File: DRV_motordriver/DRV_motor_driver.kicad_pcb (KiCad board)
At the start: 2 copper layers, 80.5 x 46.1 mm, 37 parts, among them J1 jumper, J2 jumper, J3 Conn_01x02, J4 Conn_01x02, J5 Conn_01x02, J6 Conn_01x02, J7 Conn_01x02, Q1 NMOS, Q2 NMOS, Q3 NMOS, Q4 NMOS, Q5 NMOS, Q6 NMOS, Q7 NMOS, Q8 NMOS, U1 DRV8701PRGER, U2 DRV8701PRGER

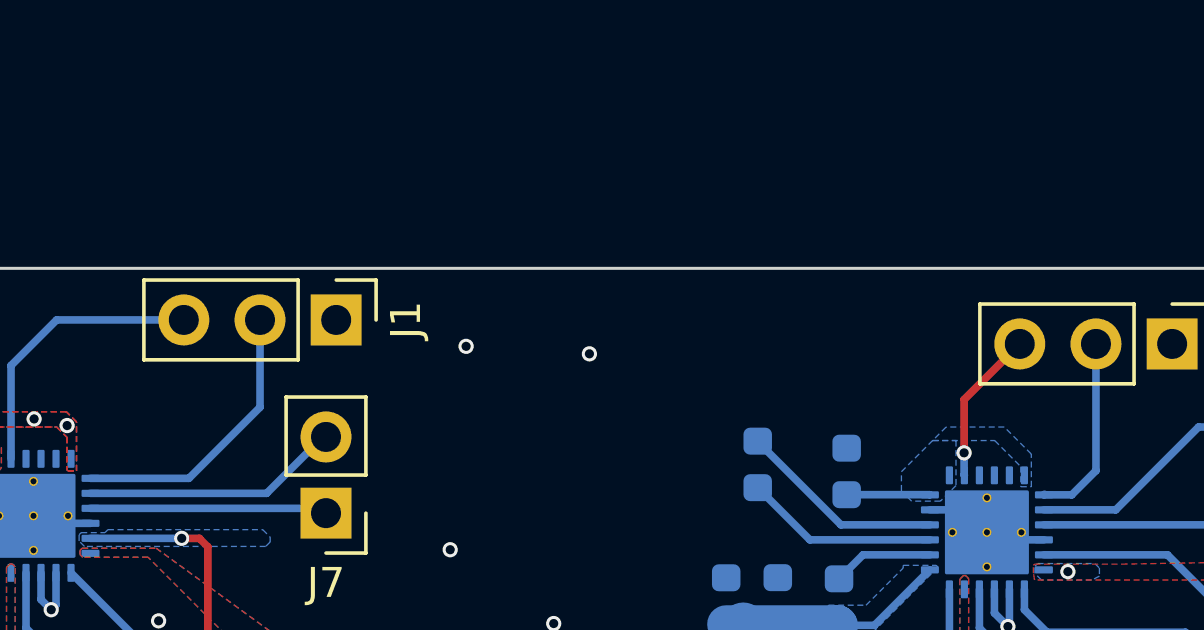
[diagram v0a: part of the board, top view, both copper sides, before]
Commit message: add readme and update on DRV motor driver
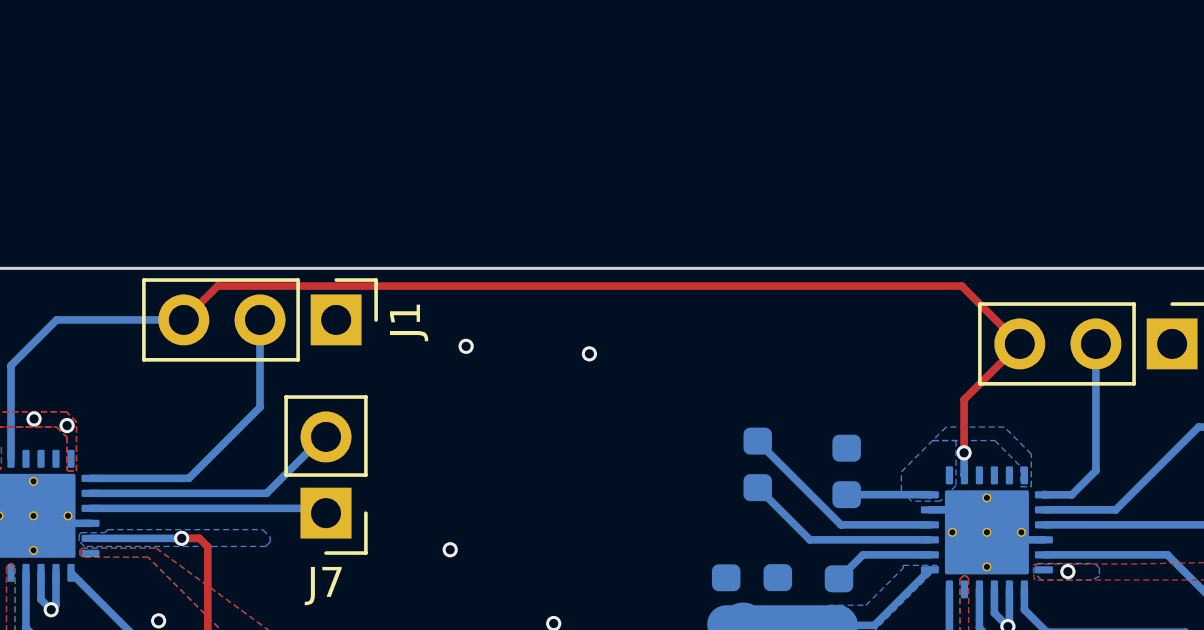
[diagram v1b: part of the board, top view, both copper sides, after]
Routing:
- net +3.3V: track 14.7 -> 43.8 mm
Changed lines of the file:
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@@
+	)
+	(segment
+		(start 77.539401 61.5806)
+		(end 76.410001 62.71)
+		(width 0.254)
+		(layer "F.Cu")
+		(net 14)
+	)
+	(segment
+		(start 102.345601 61.5806)
+		(end 77.539401 61.5806)
+		(width 0.254)
+		(layer "F.Cu")
+		(net 14)
 	)
 	(segment
@@
 		(width 0.254)
 		(layer "F.Cu")
+		(net 14)
+	)
+	(segment
+		(start 104.275001 63.51)
+		(end 102.345601 61.5806)
+		(width 0.254)
+		(layer "F.Cu")

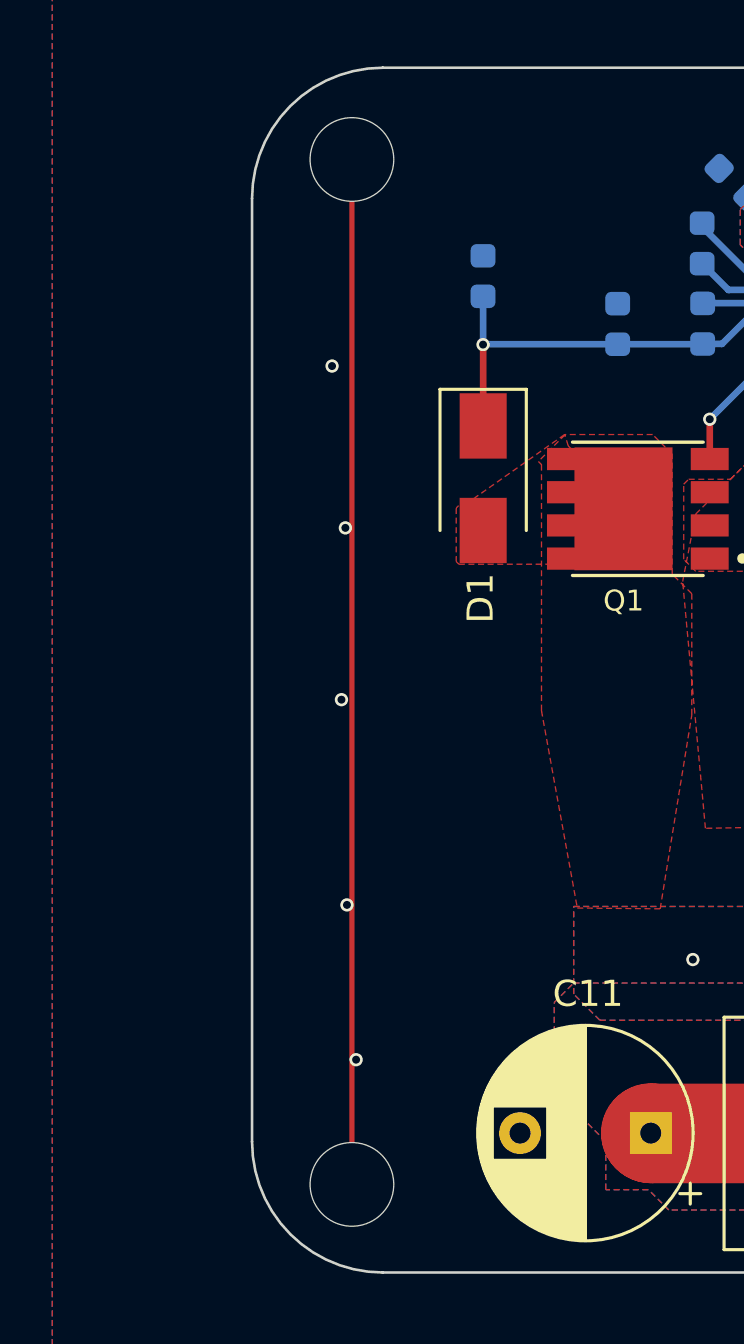
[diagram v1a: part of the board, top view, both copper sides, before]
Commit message: update library for DRV_motor_driver
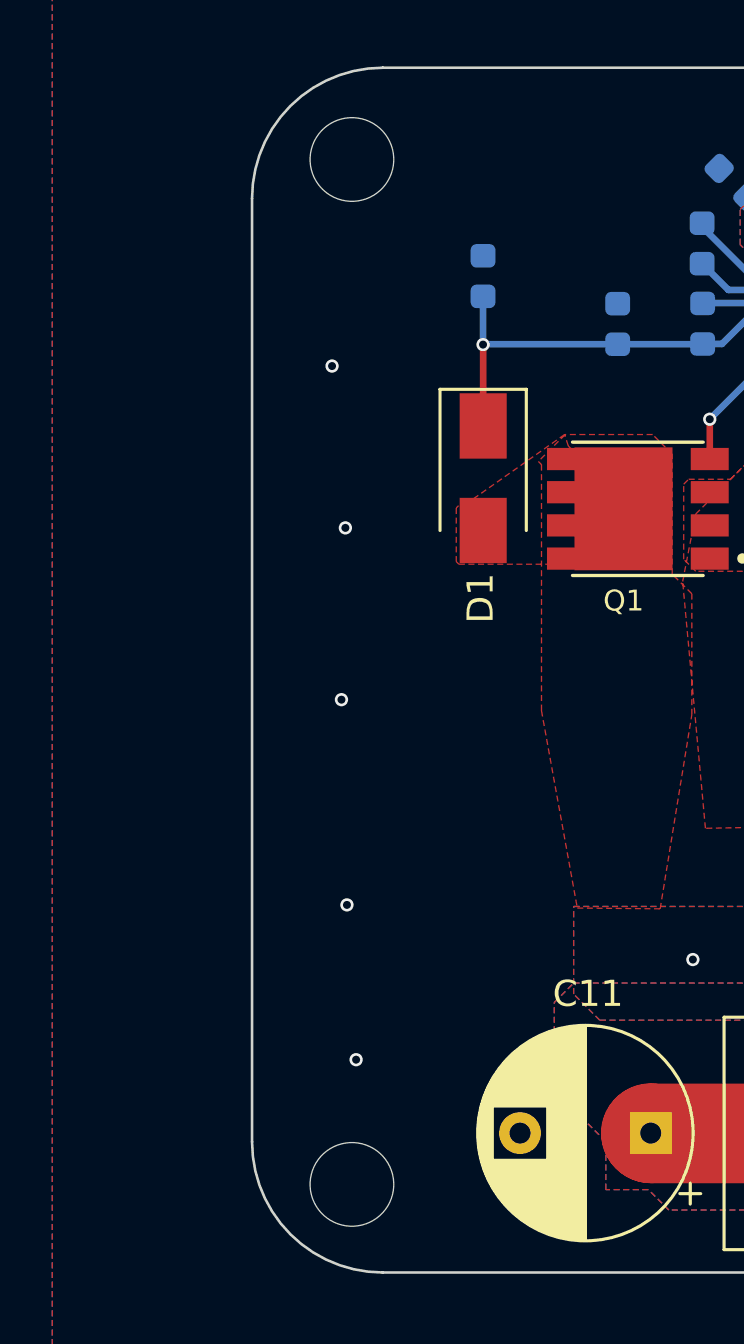
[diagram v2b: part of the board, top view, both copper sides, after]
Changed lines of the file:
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@@
-	)
-	(gr_line
-		(start 53.57 64.5)
-		(end 53.57 103.7)
-		(stroke
-			(width 0.2)
-			(type default)
-		)
-		(layer "F.Cu")
-		(net 1)
 	)
 	(gr_line
@@
 		)
 	)
-	(dimension
-		(type aligned)
-		(layer "F.Cu")
-		(pts
-			(xy 54.75 107.07) (xy 54.75 60.99)
-		)
-		(height -10.73)
-		(gr_text "46.0800 mm"
-			(at 42.22 84.03 90)
-			(layer "F.Cu")
-			(effects
-				(font
-					(size 1.5 1.5)
-					(thickness 0.3)
-				)
-			)
-		)
-		(format
-			(prefix "")
-			(suffix "")
-			(units 3)
-			(units_format 1)
-			(precision 4)
-		)
-		(style
-			(thickness 0.2)
-			(arrow_length 1.27)
-			(text_position_mode 0)
-			(extension_height 0.58642)
-			(extension_offset 0.5) keep_text_aligned)
-	)
-	(dimension
-		(type aligned)
-		(layer "F.Cu")
-		(pts
-			(xy 49.75 65.99) (xy 130.24 65.99)
-		)
-		(height -5.89)
-		(gr_text "80.4900 mm"
-			(at 89.995 58.3 0)
-			(layer "F.Cu")
-			(effects
-				(font
-					(size 1.5 1.5)
-					(thickness 0.3)
-				)
-			)
-		)
-		(format
-			(prefix "")
-			(suffix "")
-			(units 3)
-			(units_format 1)
-			(precision 4)
-		)
-		(style
-			(thickness 0.2)
-			(arrow_length 1.27)
-			(text_position_mode 0)
-			(extension_height 0.58642)
-			(extension_offset 0.5) keep_text_aligned)
-	)
 	(via
